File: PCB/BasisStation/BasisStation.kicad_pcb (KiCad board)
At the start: 2 copper layers, 19.8 x 12.9 mm, 21 parts, among them SW1 SW_SPST, SW2 RESET_BUTTON, U1 ESP32-S3-WROOM-1-N16R8, X2 JTAG

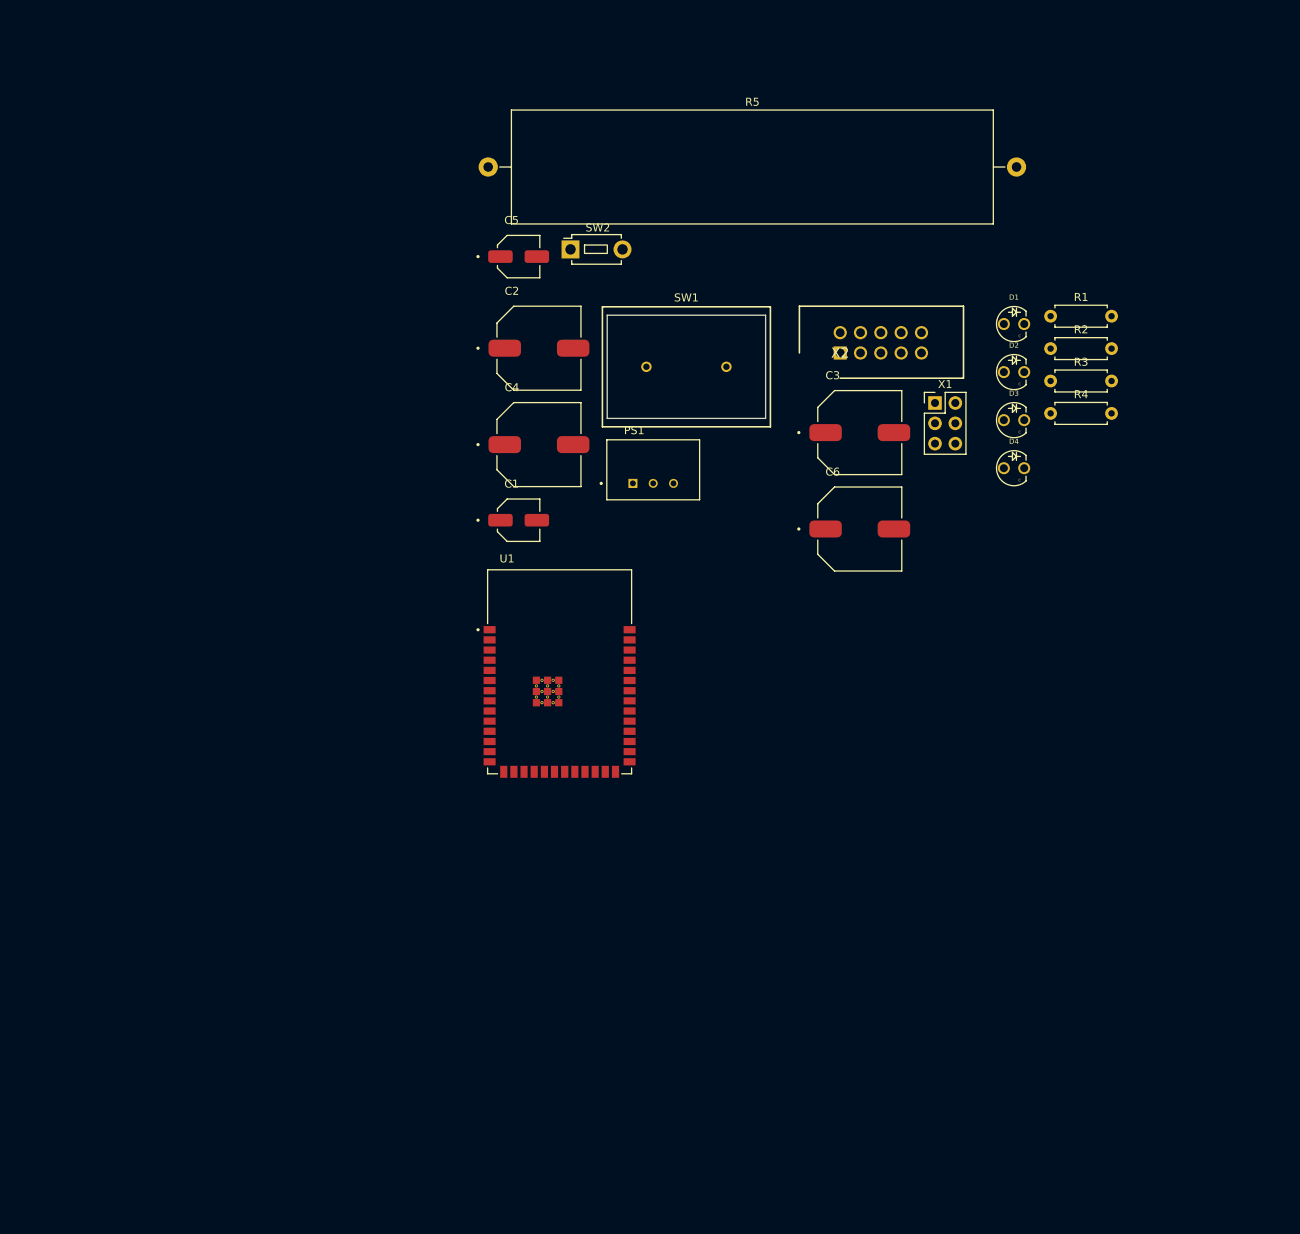
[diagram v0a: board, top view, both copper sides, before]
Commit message: neue Bauteile hinzugefügt
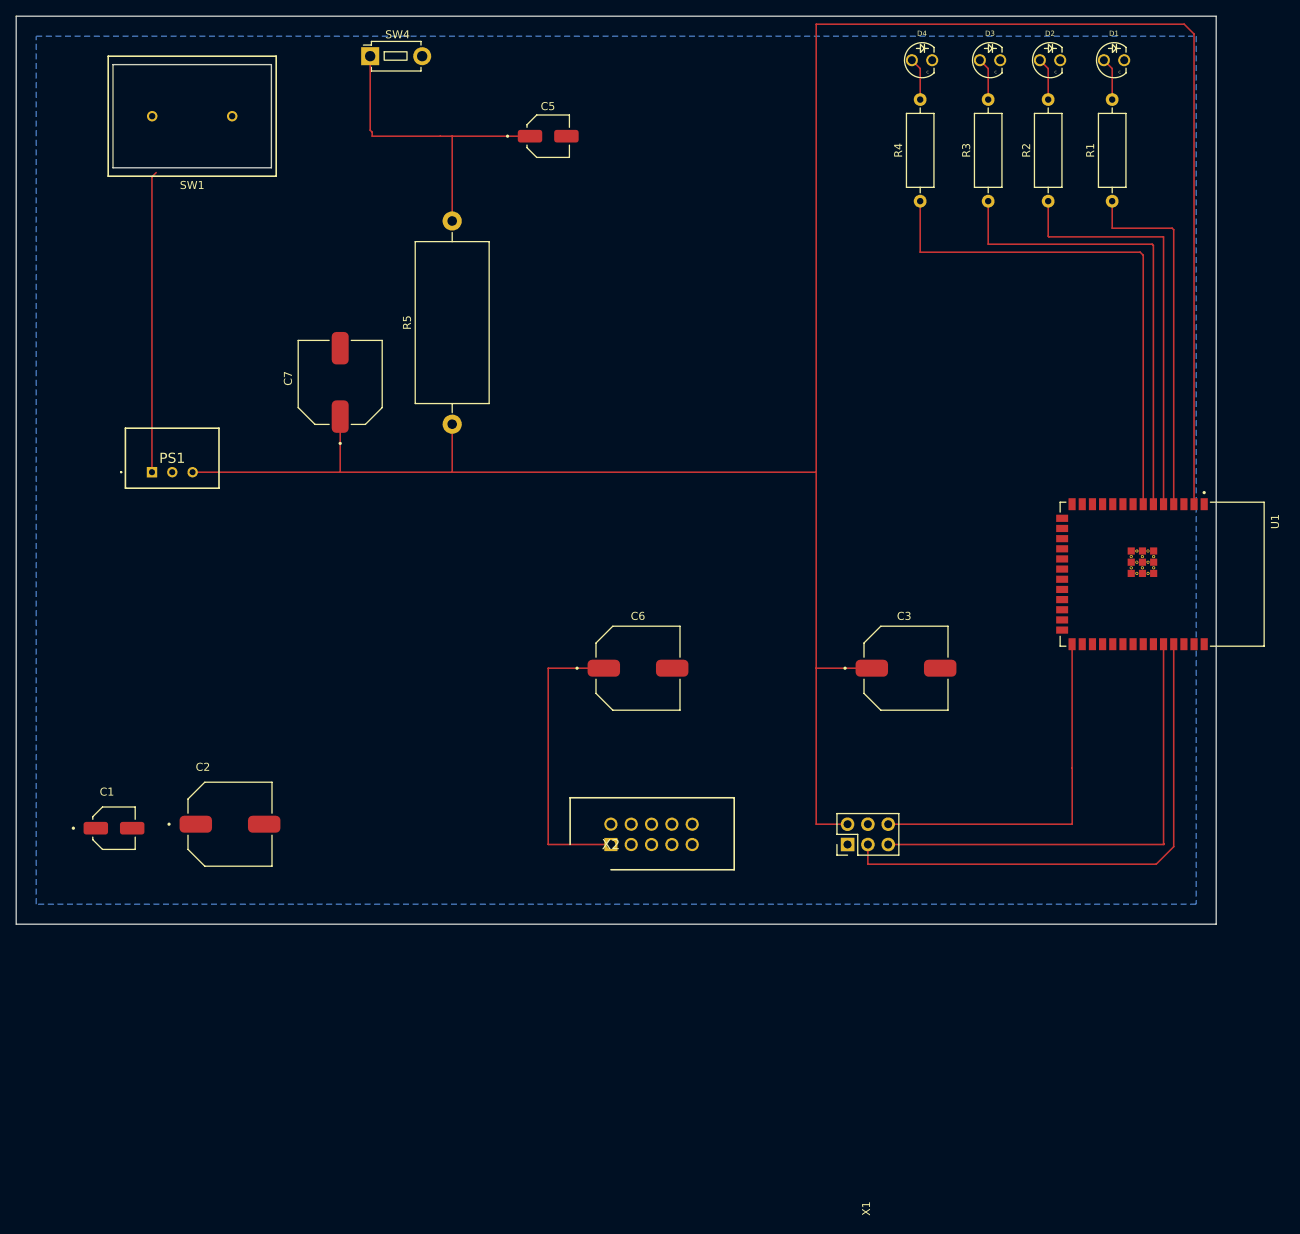
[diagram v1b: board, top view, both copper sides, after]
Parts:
- PS1: footprint Template:CONV_TSR_1-2433E -> TSR1-2433:TSR12433
- R1, R2, R3, R4: footprint Resistor_THT:R_Axial_DIN0207_L6.3mm_D2.5mm_P7.62mm_Horizontal -> Resistor_THT:R_Axial_DIN0309_L9.0mm_D3.2mm_P12.70mm_Horizontal
- R5: footprint Resistor_THT:R_Axial_Power_L60.0mm_W14.0mm_P66.04mm -> Resistor_THT:R_Axial_DIN0922_L20.0mm_D9.0mm_P25.40mm_Horizontal
- moved U1 76.3 mm to (193.2, 100.2), turned to -90 degrees
- moved C2 70.9 mm to (76.7, 131.5)
- moved SW1 69.3 mm to (72.0, 43.0), turned to 180 degrees
- moved X2 67.8 mm to (124.3, 134.0)
- moved C1 63.6 mm to (62.2, 132.0)
- moved PS1 62.7 mm to (67.0, 87.5)
- moved X1 56.3 mm to (153.9, 134.0), turned to 90 degrees
- moved D4 52.3 mm to (163.2, 36.0)
- moved D3 45.1 mm to (171.7, 36.0)
- moved D2 39.2 mm to (179.2, 36.0)
- moved D1 35.3 mm to (187.2, 36.0)
- moved SW4 34.8 mm to (94.2, 35.5)
- moved C6 32.7 mm to (127.7, 112.0)
- moved R5 32.5 mm to (104.5, 81.5), turned to 90 degrees
- moved R4 31.1 mm to (163.0, 53.6), turned to 90 degrees
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- renumbered C4 to C7, SW2 to SW4
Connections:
- C3 pad N: (no net) -> GND
- C3 pad P: (no net) -> +3.3V
- C5 pad N: (no net) -> GND
- C5 pad P: (no net) -> 3,3V
- C6 pad N: (no net) -> GND
- C6 pad P: (no net) -> +3.3V
- C7 pad N: (no net) -> GND
- C7 pad P: (no net) -> +3.3V
- PS1 pad 1: Net-(PS1-+VIN) -> +12V
- PS1 pad 3: 3,3V -> +3.3V
- SW1 pad 2: Net-(PS1-+VIN) -> +12V
- SW4 pad 1: GND -> 3,3V
- U1 pad 2: 3,3V -> +3.3V
- U1 pad 3: 3,3V -> EN
- X1 pad 1: 3,3V -> EN
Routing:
- net +3.3V: track 0.00 -> 345.1 mm
- net TX0: track 0.00 -> 66.9 mm
- net LED GREEN: track 0.00 -> 65.5 mm
- net RX0: track 0.00 -> 59.5 mm
- net LED YELLOW: track 0.00 -> 58.4 mm
- net LED RED: track 0.00 -> 52.3 mm
- net Boot Mode: track 0.00 -> 45.5 mm
- net LED BLUE: track 0.00 -> 45.5 mm
- net 3,3V: track 0.00 -> 40.4 mm
- net +12V: track 0.00 -> 37.7 mm
- net Net-(D4-A): track 0.00 -> 5.35 mm
- net Net-(D3-A): track 0.00 -> 5.35 mm
- net Net-(D2-A): track 0.00 -> 5.35 mm
- net Net-(D1-A): track 0.00 -> 5.35 mm
- net GND: track 0.00 -> 0.50 mm
- added copper zone on B.Cu, net GND
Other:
- board size 19.8 x 12.9 mm -> 150 x 113.5 mm

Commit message: Anpassung der Leiterbahnen
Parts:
- removed C2: 100µF, CUSTOM_Footprint:CAPAE1030X1050N
- C1: value 4700µF -> 100µF; footprint CUSTOM_Footprint:CAPAE530X565N -> Capacitor_THT:CP_Radial_D6.3mm_P2.50mm
- C3, C6, C7: footprint CUSTOM_Footprint:CAPAE1030X1050N -> Capacitor_THT:CP_Radial_D6.3mm_P2.50mm
- C5: value 0.47µF -> 10µF; footprint CUSTOM_Footprint:CAPAE530X565N -> Capacitor_THT:CP_Radial_D6.3mm_P2.50mm
- moved C1 73.2 mm to (115.2, 81.5)
- moved C3 60.2 mm to (101.0, 112.0), turned to 180 degrees
- moved R5 5.60 mm to (104.5, 75.9)
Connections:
- R5 pad 2: 3,3V -> +3.3V
- SW4 pad 1: 3,3V -> +3.3V
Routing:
- net EN: track 0.00 -> 168.6 mm, vias 0 -> 2
- net +3.3V: track 345.1 -> 481.8 mm
- net MTMS: track 0.00 -> 114.8 mm, vias 0 -> 2
- net MTCK: track 0.00 -> 74.9 mm, vias 0 -> 2
- net MTDO: track 0.00 -> 73.8 mm, vias 0 -> 2
- net MTDI: track 0.00 -> 72.7 mm, vias 0 -> 2
- net 3,3V: track 40.4 -> 0.00 mm
- net RX0: track 59.5 -> 47.2 mm
- net TX0: track 66.9 -> 54.6 mm
- net Boot Mode: track 45.5 -> 35.0 mm
- net GND: track 0.50 -> 6.50 mm, vias 0 -> 2
